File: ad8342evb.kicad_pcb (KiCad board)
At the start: 4 copper layers, 100 x 100 mm, 95 parts, among them J1 PWR_in_direct, J10 Bat, J11 3V3, J12 PWR_Jumper, J13 TP1, J14 TP1, J15 TP_PWR, J16 TP2, J17 TP3, J2 RF_in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

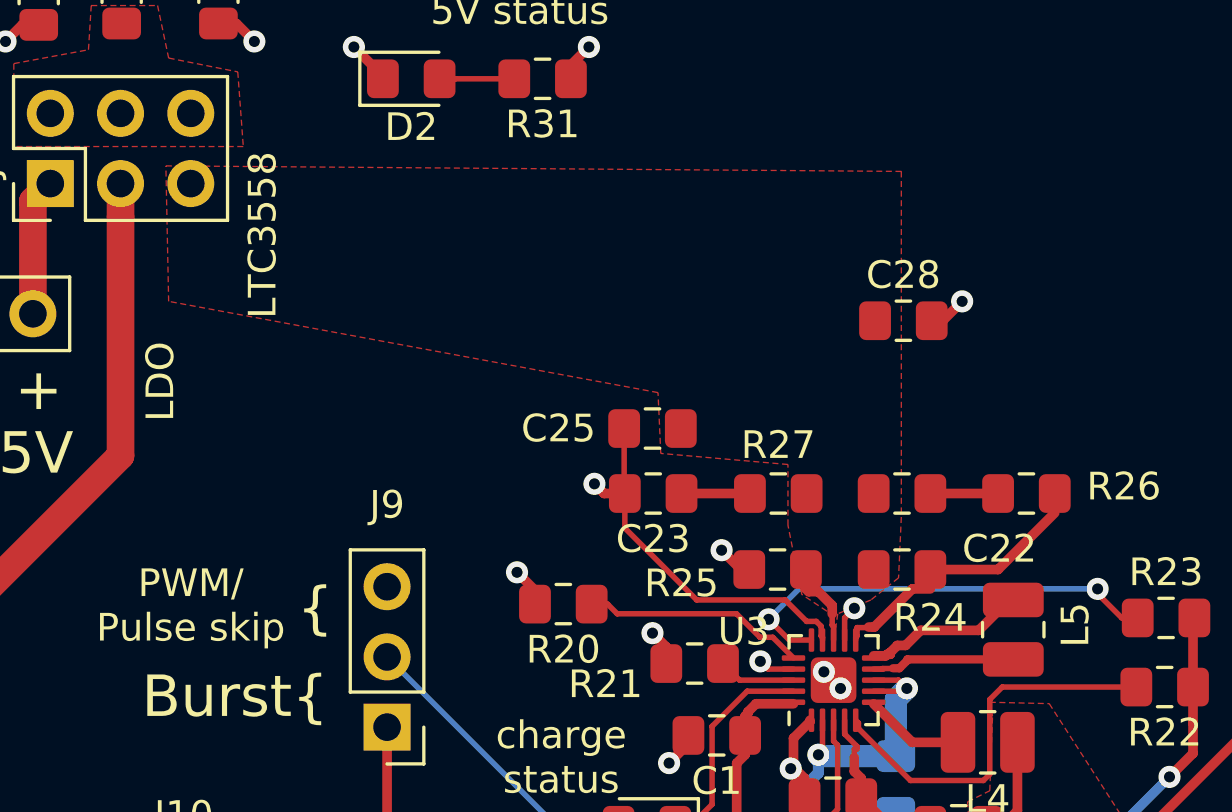
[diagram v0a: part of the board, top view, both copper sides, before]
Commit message: fixed mistake in schematic
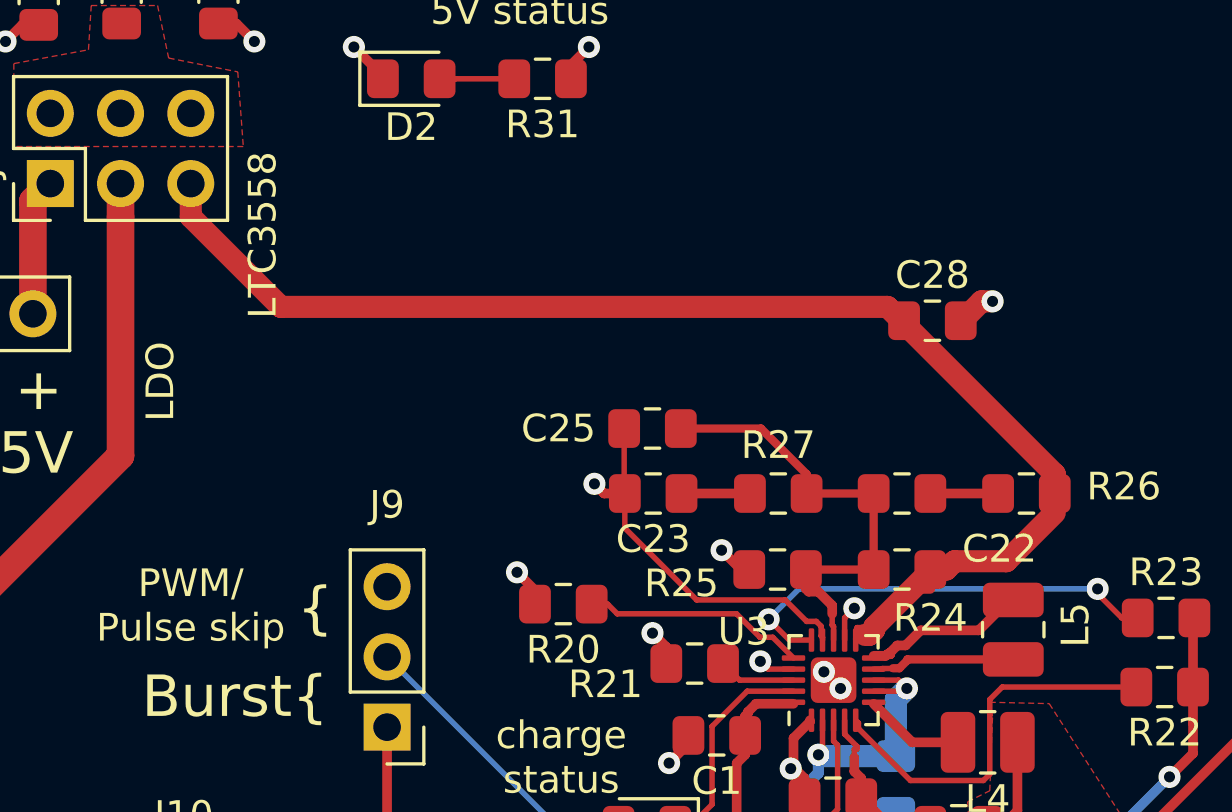
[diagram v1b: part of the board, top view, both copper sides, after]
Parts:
- moved C28 1.05 mm to (182.8, 115.5)
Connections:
- C22 pad 2: /5V_Switching -> Net-(C22-Pad2)
- C25 pad 1: /5V_Switching -> Net-(C22-Pad2)
- R24 pad 1: Net-(R24-Pad1) -> /5V_Switching
- R24 pad 2: /5V_Switching -> Net-(C22-Pad2)
- R25 pad 1: /5V_Switching -> Net-(C22-Pad2)
- R26 pad 1: Net-(R24-Pad1) -> /5V_Switching
- R27 pad 1: /5V_Switching -> Net-(C22-Pad2)
- U3 pad 11: Net-(R24-Pad1) -> /5V_Switching
- U3 pad 13: /5V_Switching -> Net-(C22-Pad2)
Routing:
- net /5V_Switching: track 3.17 -> 50.9 mm
- net Net-(C22-Pad2): track 0.00 -> 16.7 mm
- net Net-(R24-Pad1): track 10.4 -> 0.00 mm
- removed copper zone on F.Cu, net /5V_Switching

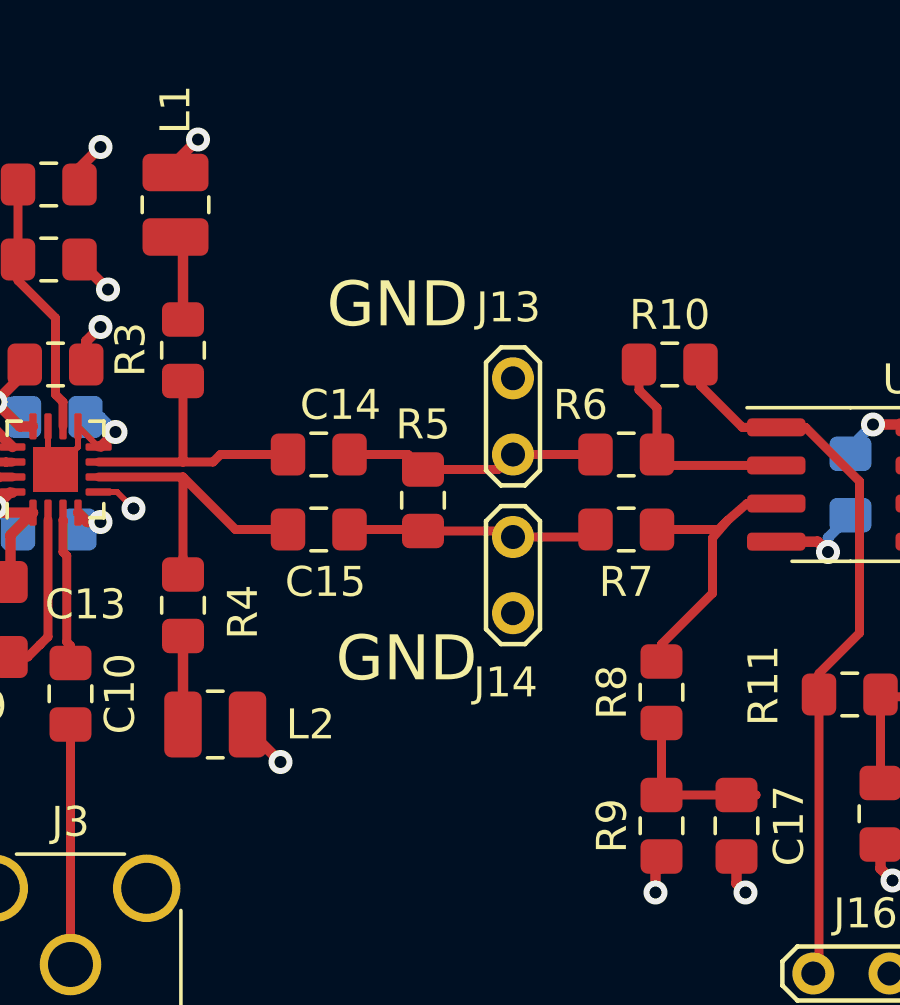
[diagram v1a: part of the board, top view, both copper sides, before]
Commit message: added DC bias resistor for OPAMP
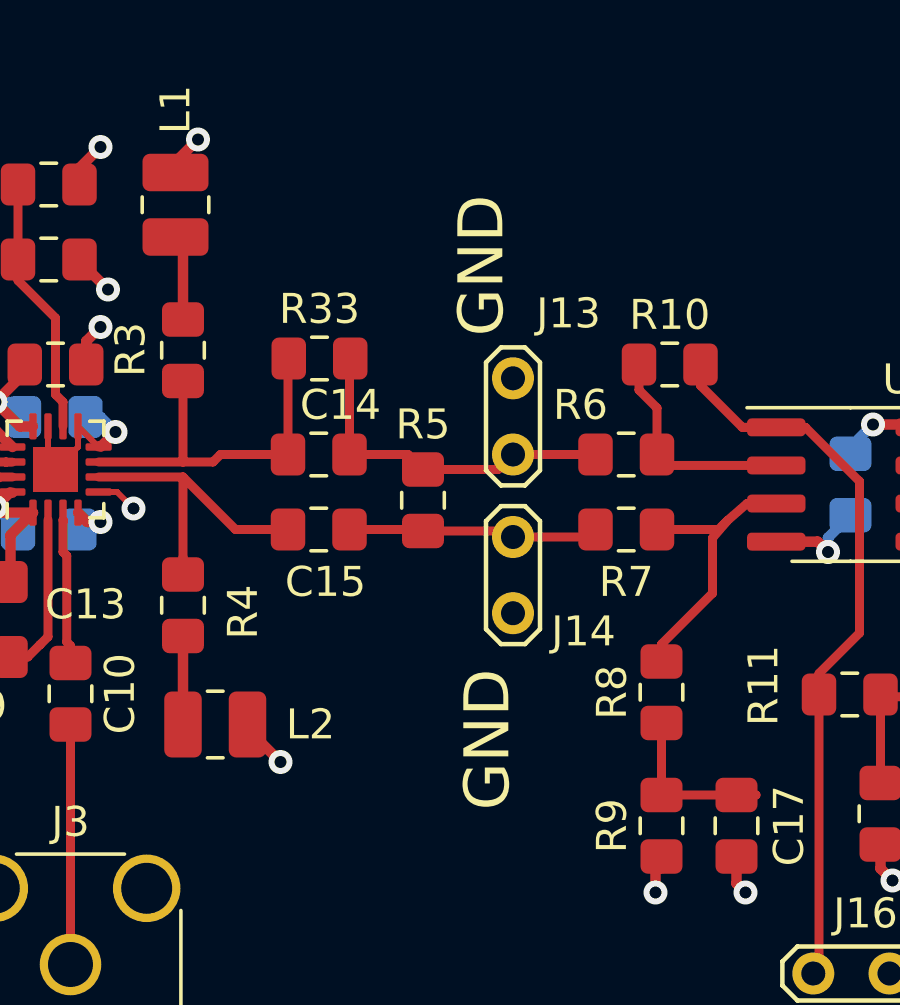
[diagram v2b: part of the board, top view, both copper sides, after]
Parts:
- added R33: 10k, Resistor_SMD:R_0805_2012Metric_Pad1.15x1.40mm_HandSolder, F.Cu at (146.3, 70.8)
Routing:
- net Net-(C14-Pad1): track 9.12 -> 12.3 mm
- net Net-(C14-Pad2): track 8.61 -> 11.8 mm
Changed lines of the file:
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@@
     (thickness 1.6)
     (drawings 40)
-    (tracks 568)
+    (tracks 572)
     (zones 0)
-    (modules 95)
+    (modules 96)
     (nets 59)
   )
@@
     (add_net "Net-(L4-Pad2)")
   )
+  (module Resistor_SMD:R_0805_2012Metric_Pad1.15x1.40mm_HandSolder (layer F.Cu)
+    (at 146.3 70.8)
+    (descr "Resistor SMD 0805 (2012 Metric), square (rectangular) end terminal, IPC_7351 nominal with elongated pad for handsoldering. (Body size source: https://docs.google.com/spreadsheets/d/1BsfQQcO9C6DZCsRaXUlFlo91Tg2WpOkGARC1WS5S8t0/edit?usp=sharing), generated with kicad-footprint-generator")
+    (tags "resistor handsolder")
+    (attr smd)
+    (fp_text reference R33 (at 0 -1.65) (layer F.SilkS)
+      (effects (font (size 1 1) (thickness 0.15)))
+    )
+    (fp_text value 10k (at 0 1.65) (layer F.Fab)
+      (effects (font (size 1 1) (thickness 0.15)))
+    )
+    (fp_text user %R (at 0 0) (layer F.Fab)
+      (effects (font (size 0.5 0.5) (thickness 0.08)))
+    )
+    (fp_line (start 1.85 0.95) (end -1.85 0.95) (layer F.CrtYd) (width 0.05))
+    (fp_line (start 1.85 -0.95) (end 1.85 0.95) (layer F.CrtYd) (width 0.05))
+    (fp_line (start -1.85 -0.95) (end 1.85 -0.95) (layer F.CrtYd) (width 0.05))
+    (fp_line (start -1.85 0.95) (end -1.85 -0.95) (layer F.CrtYd) (width 0.05))
+    (fp_line (start -0.261252 0.71) (end 0.261252 0.71) (layer F.SilkS) (width 0.12))
+    (fp_line (start -0.261252 -0.71) (end 0.261252 -0.71) (layer F.SilkS) (width 0.12))
+    (fp_line (start 1 0.6) (end -1 0.6) (layer F.Fab) (width 0.1))
+    (fp_line (start 1 -0.6) (end 1 0.6) (layer F.Fab) (width 0.1))
+    (fp_line (start -1 -0.6) (end 1 -0.6) (layer F.Fab) (width 0.1))
+    (fp_line (start -1 0.6) (end -1 -0.6) (layer F.Fab) (width 0.1))
+    (pad 2 smd roundrect (at 1.025 0) (size 1.15 1.4) (layers F.Cu F.Paste F.Mask) (roundrect_rratio 0.217391)
+      (net 35 "Net-(C14-Pad2)"))
+    (pad 1 smd roundrect (at -1.025 0) (size 1.15 1.4) (layers F.Cu F.Paste F.Mask) (roundrect_rratio 0.217391)
+      (net 29 "Net-(C14-Pad1)"))
+    (model ${KISYS3DMOD}/Resistor_SMD.3dshapes/R_0805_2012Metric.wrl
+      (at (xyz 0 0 0))
+      (scale (xyz 1 1 1))
+      (rotate (xyz 0 0 0))
+    )
+  )
   (module Inductor_SMD:L_0805_2012Metric_Pad1.15x1.40mm_HandSolder (layer F.Cu)
     (at 145.7 109.8 270)
@@
     (tags "CONN DEV")
     (attr virtual)
-    (fp_text reference J14 (at -2.31 -0.25 180) (layer F.SilkS)
+    (fp_text reference J14 (at -0.61 2.35 180) (layer F.SilkS)
       (effects (font (size 1 1) (thickness 0.15)))
     )
@@
     (tags "CONN DEV")
     (attr virtual)
-    (fp_text reference J13 (at 4.9 -0.15 180) (layer F.SilkS)
+    (fp_text reference J13 (at 4.7 1.85 180) (layer F.SilkS)
       (effects (font (size 1 1) (thickness 0.15)))
     )
@@
     (effects (font (size 1.5 1.5) (thickness 0.3)))
   )
-  (gr_text GND (at 149.2 80.8) (layer F.SilkS)
+  (gr_text GND (at 151.9 83.5 90) (layer F.SilkS)
     (effects (font (size 1.5 1.5) (thickness 0.3)))
   )
-  (gr_text GND (at 148.9 69) (layer F.SilkS)
+  (gr_text GND (at 151.7 67.7 90) (layer F.SilkS)
     (effects (font (size 1.5 1.5) (thickness 0.3)))
   )
@@
   (via (at 176.9 126.3) (size 0.8) (drill 0.4) (layers F.Cu B.Cu) (net 17))
   (segment (start 177.65 127.05) (end 176.9 126.3) (width 0.2) (layer F.Cu) (net 17))
-  (segment (start 179.25 126.558294) (end 179.2 126.508294) (width 0.2) (layer F.Cu) (net 58))
-  (segment (start 179.25 127.05) (end 179.25 126.558294) (width 0.2) (layer F.Cu) (net 58))
-  (segment (start 179.2 126.508294) (end 179.2 126.1) (width 0.2) (layer F.Cu) (net 58))
-  (segment (start 179.2 126.1) (end 179.2 125.8) (width 0.35) (layer F.Cu) (net 58))
-  (segment (start 179.2 125.8) (end 178.7 125.3) (width 0.35) (layer F.Cu) (net 58))
-  (segment (start 178.25 125.2) (end 178.25 124.5) (width 0.35) (layer F.Cu) (net 58))
-  (segment (start 178.35 125.3) (end 178.25 125.2) (width 0.35) (layer F.Cu) (net 58))
-  (segment (start 178.7 125.3) (end 178.35 125.3) (width 0.35) (layer F.Cu) (net 58))
   (segment (start 187.25 121.75) (end 187.25 122.45) (width 0.2) (layer F.Cu) (net 18))
   (segment (start 182.75 124.5) (end 182.75 125.2) (width 0.2) (layer F.Cu) (net 18))
@@
   (segment (start 142.75 74.25) (end 141.75 74.25) (width 0.3) (layer F.Cu) (net 29))
   (segment (start 141.75 74.25) (end 138.9375 74.25) (width 0.3) (layer F.Cu) (net 29))
+  (segment (start 145.25 70.825) (end 145.275 70.8) (width 0.3) (layer F.Cu) (net 29))
+  (segment (start 145.25 74) (end 145.25 70.825) (width 0.3) (layer F.Cu) (net 29))
   (segment (start 145.25 76.5) (end 143.5 76.5) (width 0.3) (layer F.Cu) (net 30))
   (segment (start 141.75 74.75) (end 138.9375 74.75) (width 0.3) (layer F.Cu) (net 30))
@@
   (segment (start 149.75 74.5) (end 152.25 74.5) (width 0.3) (layer F.Cu) (net 35))
   (segment (start 152.75 74) (end 155.5 74) (width 0.3) (layer F.Cu) (net 35))
+  (segment (start 147.3 70.825) (end 147.325 70.8) (width 0.3) (layer F.Cu) (net 35))
+  (segment (start 147.3 74) (end 147.3 70.825) (width 0.3) (layer F.Cu) (net 35))
   (segment (start 149.7 76.5) (end 149.75 76.55) (width 0.3) (layer F.Cu) (net 36))
   (segment (start 147.3 76.5) (end 149.7 76.5) (width 0.3) (layer F.Cu) (net 36))
@@
   (segment (start 171.675 121.725) (end 171.7 121.75) (width 0.2) (layer F.Cu) (net 57))
   (segment (start 171.675 119.4) (end 171.675 121.725) (width 0.2) (layer F.Cu) (net 57))
+  (segment (start 179.25 126.558294) (end 179.2 126.508294) (width 0.2) (layer F.Cu) (net 58))
+  (segment (start 179.25 127.05) (end 179.25 126.558294) (width 0.2) (layer F.Cu) (net 58))
+  (segment (start 179.2 126.508294) (end 179.2 126.1) (width 0.2) (layer F.Cu) (net 58))
+  (segment (start 179.2 126.1) (end 179.2 125.8) (width 0.35) (layer F.Cu) (net 58))
+  (segment (start 179.2 125.8) (end 178.7 125.3) (width 0.35) (layer F.Cu) (net 58))
+  (segment (start 178.25 125.2) (end 178.25 124.5) (width 0.35) (layer F.Cu) (net 58))
+  (segment (start 178.35 125.3) (end 178.25 125.2) (width 0.35) (layer F.Cu) (net 58))
+  (segment (start 178.7 125.3) (end 178.35 125.3) (width 0.35) (layer F.Cu) (net 58))
   (segment (start 176.625 119.4) (end 178.275 121.05) (width 0.3) (layer F.Cu) (net 58))
   (segment (start 178.275 121.05) (end 178.275 121.75) (width 0.3) (layer F.Cu) (net 58))

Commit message: moved bias resistor to correct location
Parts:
- moved R33 9.20 mm to (146.3, 80.0)
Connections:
- R33 pad 1: Net-(C14-Pad1) -> Net-(C15-Pad1)
- R33 pad 2: Net-(C14-Pad2) -> Net-(C15-Pad2)
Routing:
- net Net-(C15-Pad1): track 10.3 -> 13.8 mm
- net Net-(C15-Pad2): track 8.41 -> 11.9 mm
- net Net-(C14-Pad1): track 12.3 -> 9.12 mm
- net Net-(C14-Pad2): track 11.8 -> 8.61 mm
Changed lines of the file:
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@@
   )
   (module Resistor_SMD:R_0805_2012Metric_Pad1.15x1.40mm_HandSolder (layer F.Cu)
-    (at 146.3 70.8)
+    (at 146.3 80)
     (descr "Resistor SMD 0805 (2012 Metric), square (rectangular) end terminal, IPC_7351 nominal with elongated pad for handsoldering. (Body size source: https://docs.google.com/spreadsheets/d/1BsfQQcO9C6DZCsRaXUlFlo91Tg2WpOkGARC1WS5S8t0/edit?usp=sharing), generated with kicad-footprint-generator")
     (tags "resistor handsolder")
     (attr smd)
-    (fp_text reference R33 (at 0 -1.65) (layer F.SilkS)
+    (fp_text reference R33 (at 2.2 1.8) (layer F.SilkS)
       (effects (font (size 1 1) (thickness 0.15)))
     )
@@
     (fp_line (start -1 0.6) (end -1 -0.6) (layer F.Fab) (width 0.1))
     (pad 2 smd roundrect (at 1.025 0) (size 1.15 1.4) (layers F.Cu F.Paste F.Mask) (roundrect_rratio 0.217391)
-      (net 35 "Net-(C14-Pad2)"))
+      (net 36 "Net-(C15-Pad2)"))
     (pad 1 smd roundrect (at -1.025 0) (size 1.15 1.4) (layers F.Cu F.Paste F.Mask) (roundrect_rratio 0.217391)
-      (net 29 "Net-(C14-Pad1)"))
+      (net 30 "Net-(C15-Pad1)"))
     (model ${KISYS3DMOD}/Resistor_SMD.3dshapes/R_0805_2012Metric.wrl
       (at (xyz 0 0 0))
@@
   (segment (start 142.75 74.25) (end 141.75 74.25) (width 0.3) (layer F.Cu) (net 29))
   (segment (start 141.75 74.25) (end 138.9375 74.25) (width 0.3) (layer F.Cu) (net 29))
-  (segment (start 145.25 70.825) (end 145.275 70.8) (width 0.3) (layer F.Cu) (net 29))
-  (segment (start 145.25 74) (end 145.25 70.825) (width 0.3) (layer F.Cu) (net 29))
   (segment (start 145.25 76.5) (end 143.5 76.5) (width 0.3) (layer F.Cu) (net 30))
   (segment (start 141.75 74.75) (end 138.9375 74.75) (width 0.3) (layer F.Cu) (net 30))
@@
   (segment (start 141.75 77.425) (end 141.75 74.75) (width 0.3) (layer F.Cu) (net 30))
   (segment (start 141.75 78) (end 141.75 77.425) (width 0.3) (layer F.Cu) (net 30))
+  (segment (start 145.275 76.525) (end 145.25 76.5) (width 0.3) (layer F.Cu) (net 30))
+  (segment (start 145.275 80) (end 145.275 76.525) (width 0.3) (layer F.Cu) (net 30))
   (segment (start 138 80.375) (end 137.875 80.25) (width 0.3) (layer F.Cu) (net 31))
   (segment (start 138 80.95) (end 138 80.375) (width 0.3) (layer F.Cu) (net 31))
@@
   (segment (start 149.75 74.5) (end 152.25 74.5) (width 0.3) (layer F.Cu) (net 35))
   (segment (start 152.75 74) (end 155.5 74) (width 0.3) (layer F.Cu) (net 35))
-  (segment (start 147.3 70.825) (end 147.325 70.8) (width 0.3) (layer F.Cu) (net 35))
-  (segment (start 147.3 74) (end 147.3 70.825) (width 0.3) (layer F.Cu) (net 35))
   (segment (start 149.7 76.5) (end 149.75 76.55) (width 0.3) (layer F.Cu) (net 36))
   (segment (start 147.3 76.5) (end 149.7 76.5) (width 0.3) (layer F.Cu) (net 36))
@@
   (segment (start 155.25 76.75) (end 155.5 76.5) (width 0.3) (layer F.Cu) (net 36))
   (segment (start 152.75 76.75) (end 155.25 76.75) (width 0.3) (layer F.Cu) (net 36))
+  (segment (start 147.325 76.525) (end 147.3 76.5) (width 0.3) (layer F.Cu) (net 36))
+  (segment (start 147.325 80) (end 147.325 76.525) (width 0.3) (layer F.Cu) (net 36))
   (segment (start 157.7 82.95) (end 157.7 85.35) (width 0.3) (layer F.Cu) (net 37))
   (segment (start 157.7 85.35) (end 160.85 85.35) (width 0.3) (layer F.Cu) (net 37))

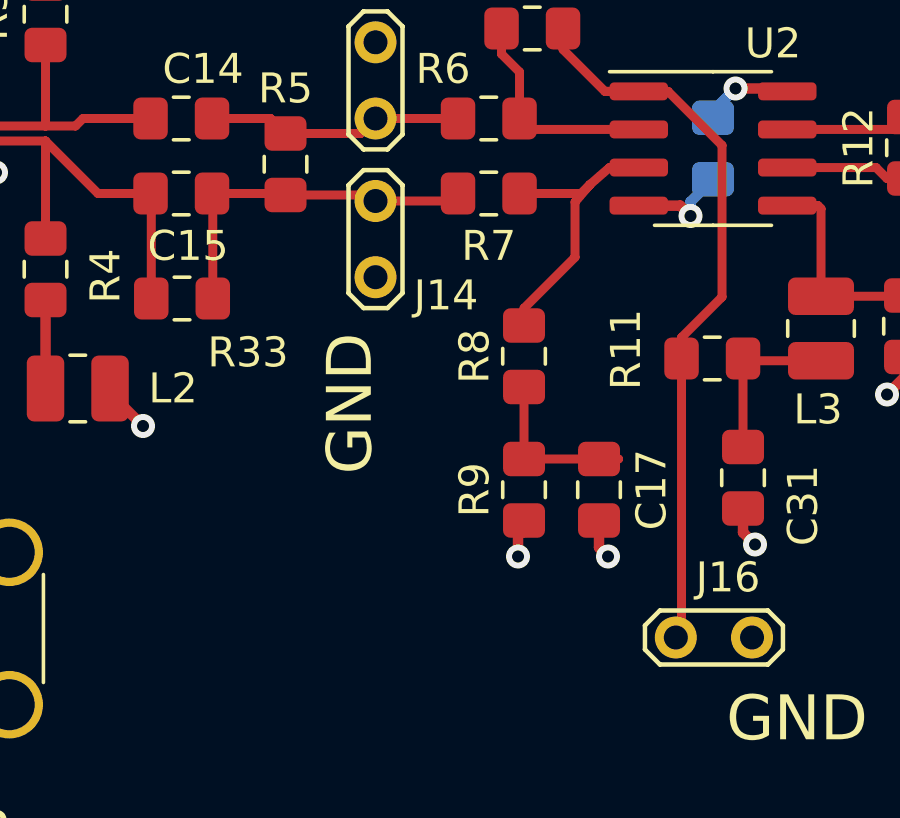
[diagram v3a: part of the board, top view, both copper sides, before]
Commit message: modified bias circuit
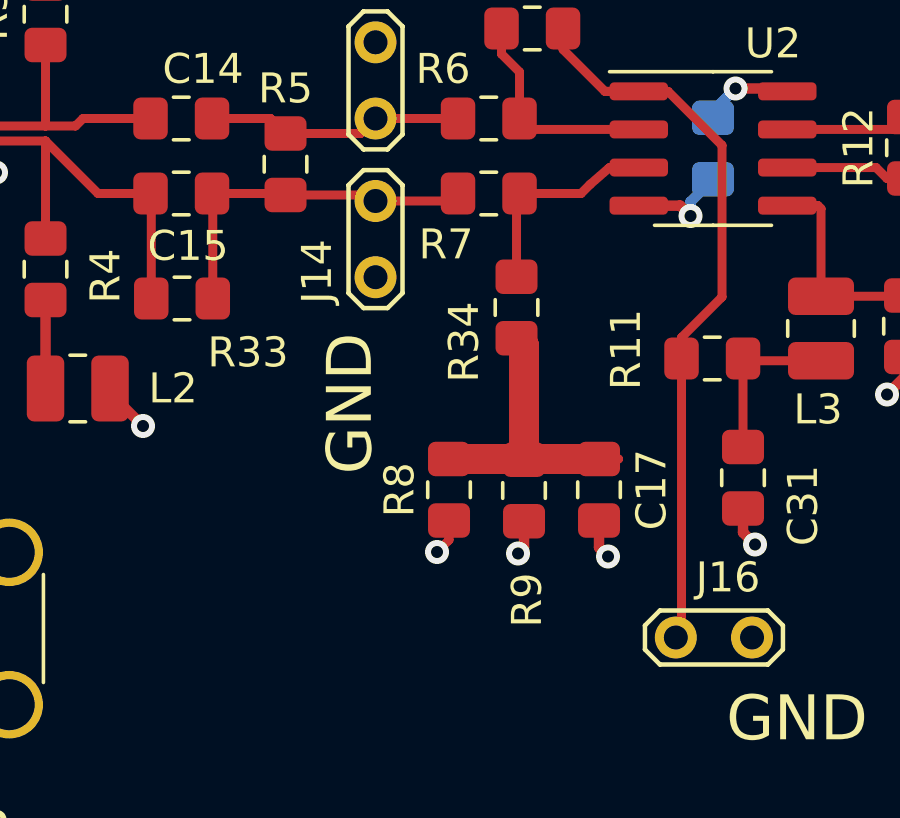
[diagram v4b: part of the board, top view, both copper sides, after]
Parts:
- added R34: 10k, Resistor_SMD:R_0805_2012Metric_Pad1.15x1.40mm_HandSolder, F.Cu at (157.4, 80.3)
- R33: value 10k -> x
- R8, R9: value 4k7 -> 10k
- moved R8 5.10 mm to (155.2, 86.4)
- turned R9 to 270 degrees
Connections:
- R7 pad 2: Net-(R7-Pad2) -> Net-(R34-Pad2)
- R8 pad 1: Net-(C17-Pad2) -> GNDA
- R8 pad 2: Net-(R7-Pad2) -> Net-(C17-Pad2)
- R9 pad 1: GNDA -> Net-(C17-Pad2)
- R9 pad 2: Net-(C17-Pad2) -> +5V
- U2 pad 3: Net-(R7-Pad2) -> Net-(R34-Pad2)
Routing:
- net Net-(R7-Pad2): track 9.90 -> 0.00 mm
- net Net-(C17-Pad2): track 6.20 -> 15.5 mm
- net Net-(R34-Pad2): track 0.00 -> 7.13 mm
- net +5V: track 28.3 -> 29.4 mm, vias 10 -> 11
- net GNDA: track 47.9 -> 47.1 mm
